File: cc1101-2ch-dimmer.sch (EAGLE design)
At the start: 24 parts, among them Q1 IRLZ44, Q2 IRLZ44, U1 ATMEGA328P-AU, U2 0ZCG0035AF2C, U3 173950378, X2 MSTBA2, X3 MSTBA2, X4 MSTBA2

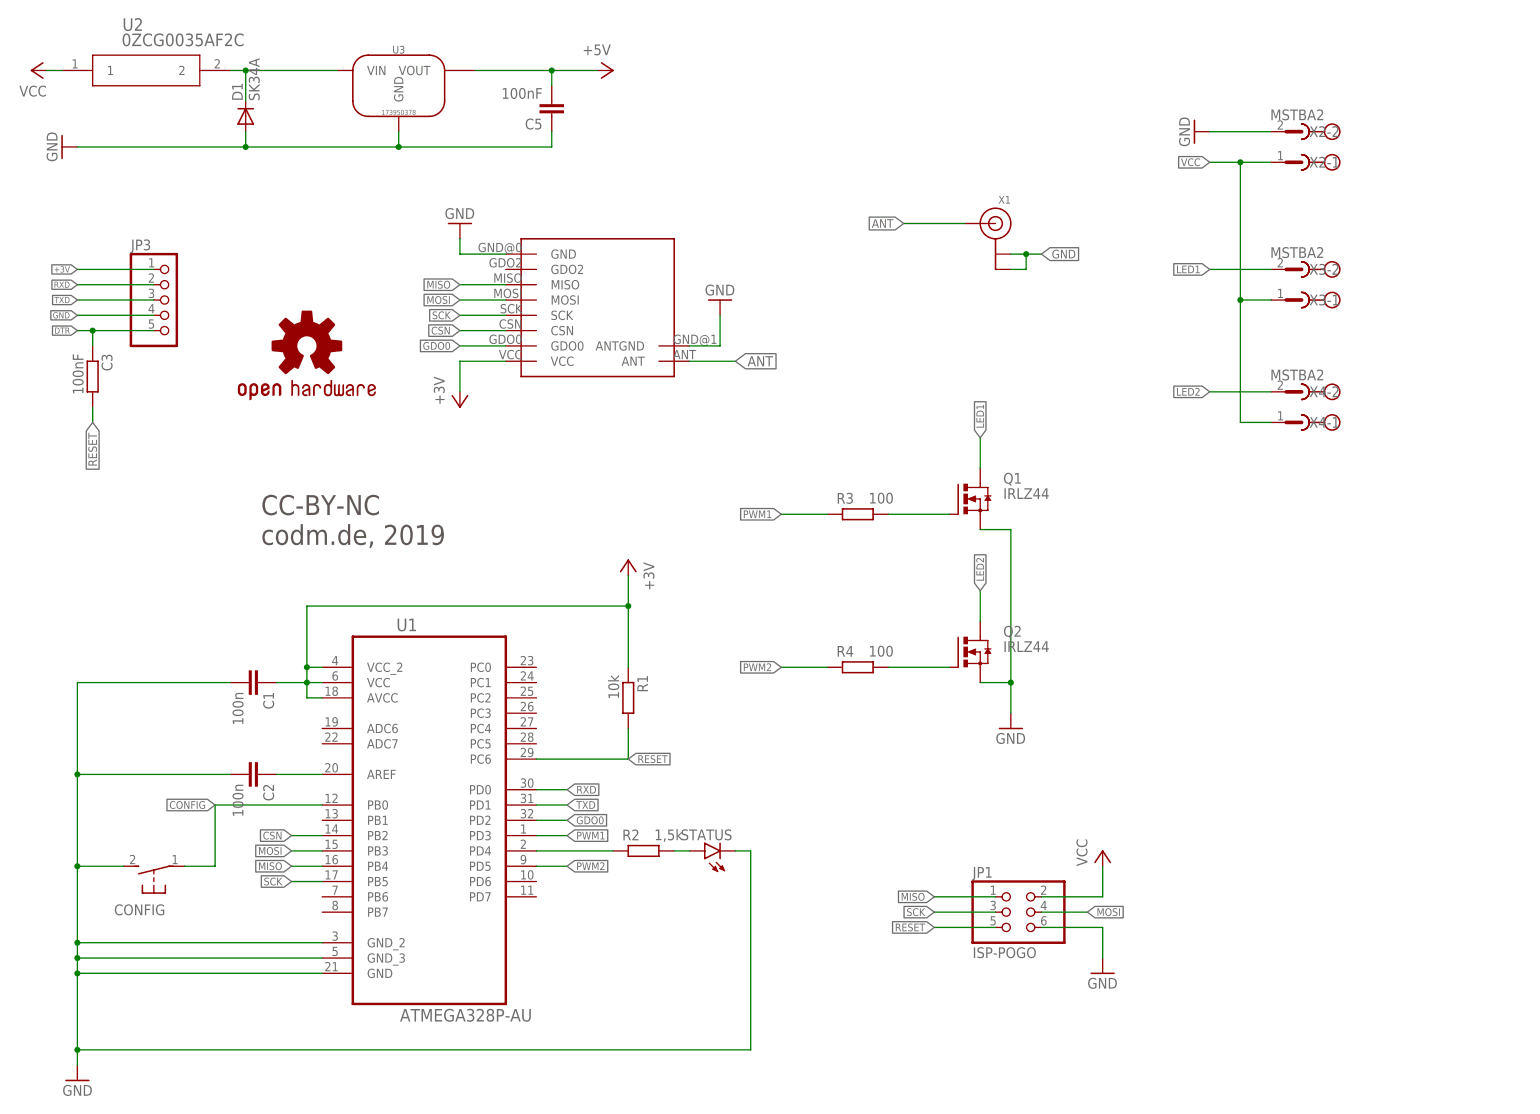
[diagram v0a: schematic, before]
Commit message: added 8mhz resonator, reworked for 0.2
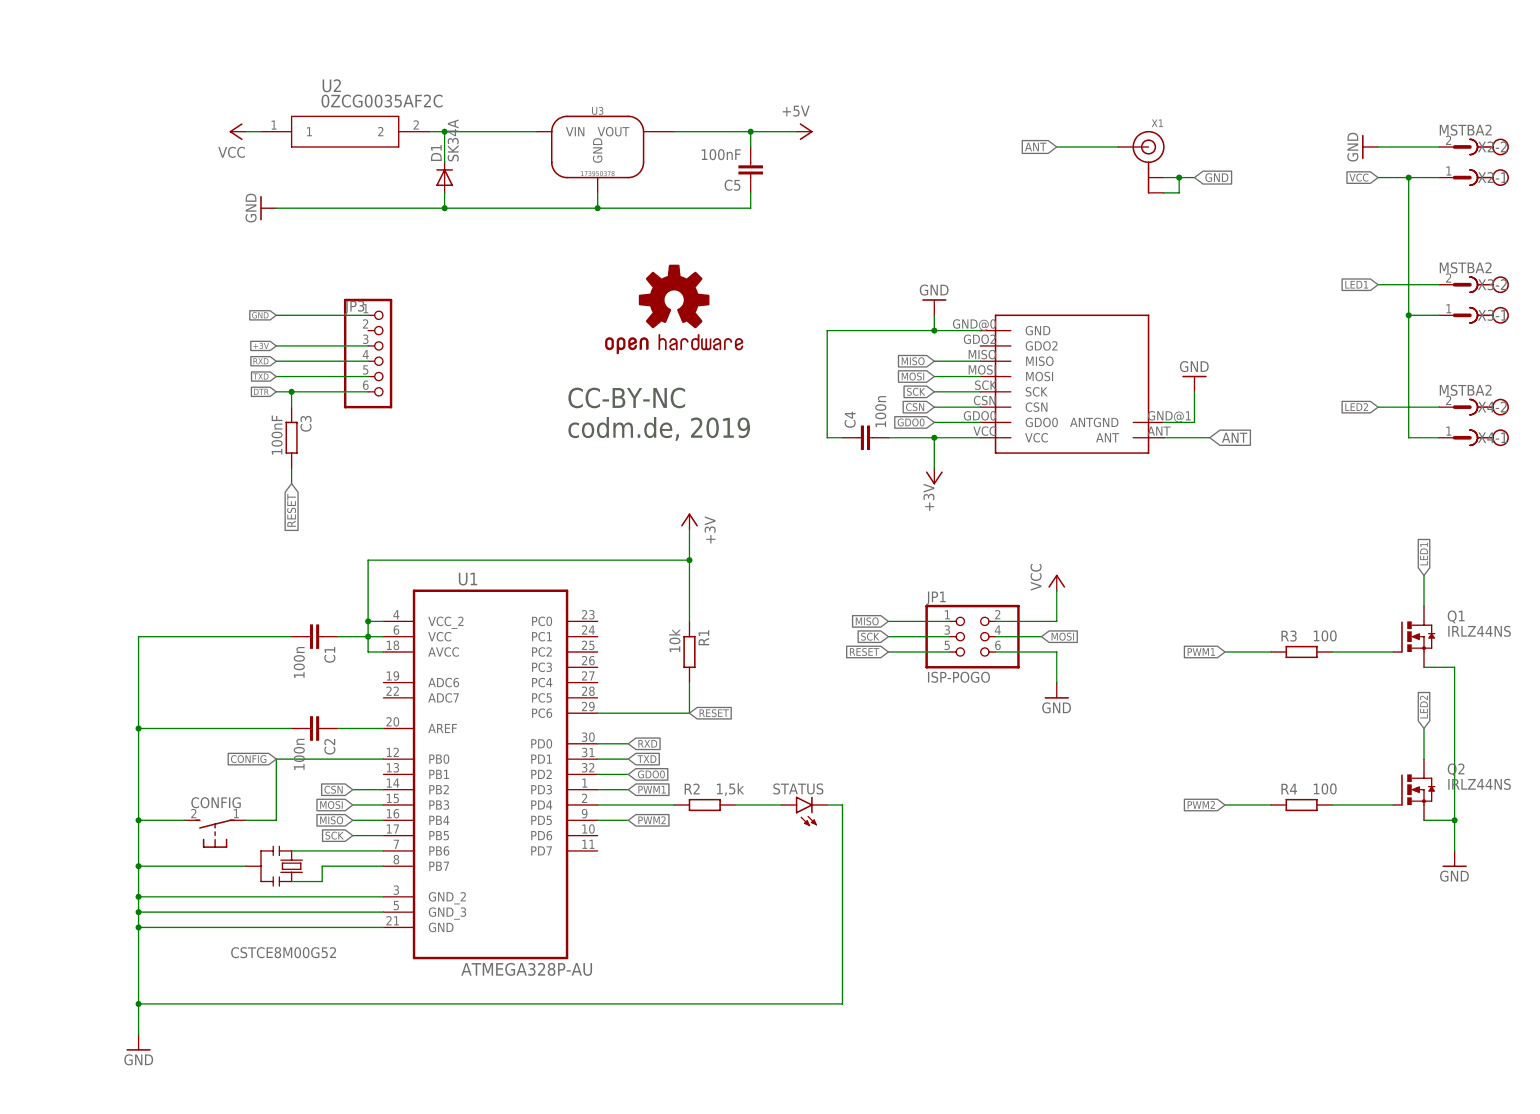
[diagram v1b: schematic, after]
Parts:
- added C4: 100n, rcl:C-EUC0805
- added Y1: CSTCE8M00G52, SmartPrj:RESONATORMU
- JP3: device pinhead:PINHD-1X5 -> pinhead:PINHD-1X6
- Q1, Q2: value IRLZ44 -> IRLZ44NS; device codm:IRFR4105ZPBF -> codm:IRLZ44NSD2PAK
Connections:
- new net N$4: U1.PB6, Y1.1
- new net N$7: U1.PB7, Y1.3
- net +3V: now also C4.2, JP3.3; no longer JP3.1
- net DTR: now also JP3.6; no longer JP3.5
- net GND: now also C4.1, JP3.1, Y1.2; no longer JP3.4
- net RXD: now also JP3.4; no longer JP3.2
- net TXD: now also JP3.5; no longer JP3.3
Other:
- moved on the sheet: C1, C2, C3, C5, CONFIG, D1, JP1, Q1, Q2, R1, R2, R3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

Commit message: reworked clearance, used newer aisler dru
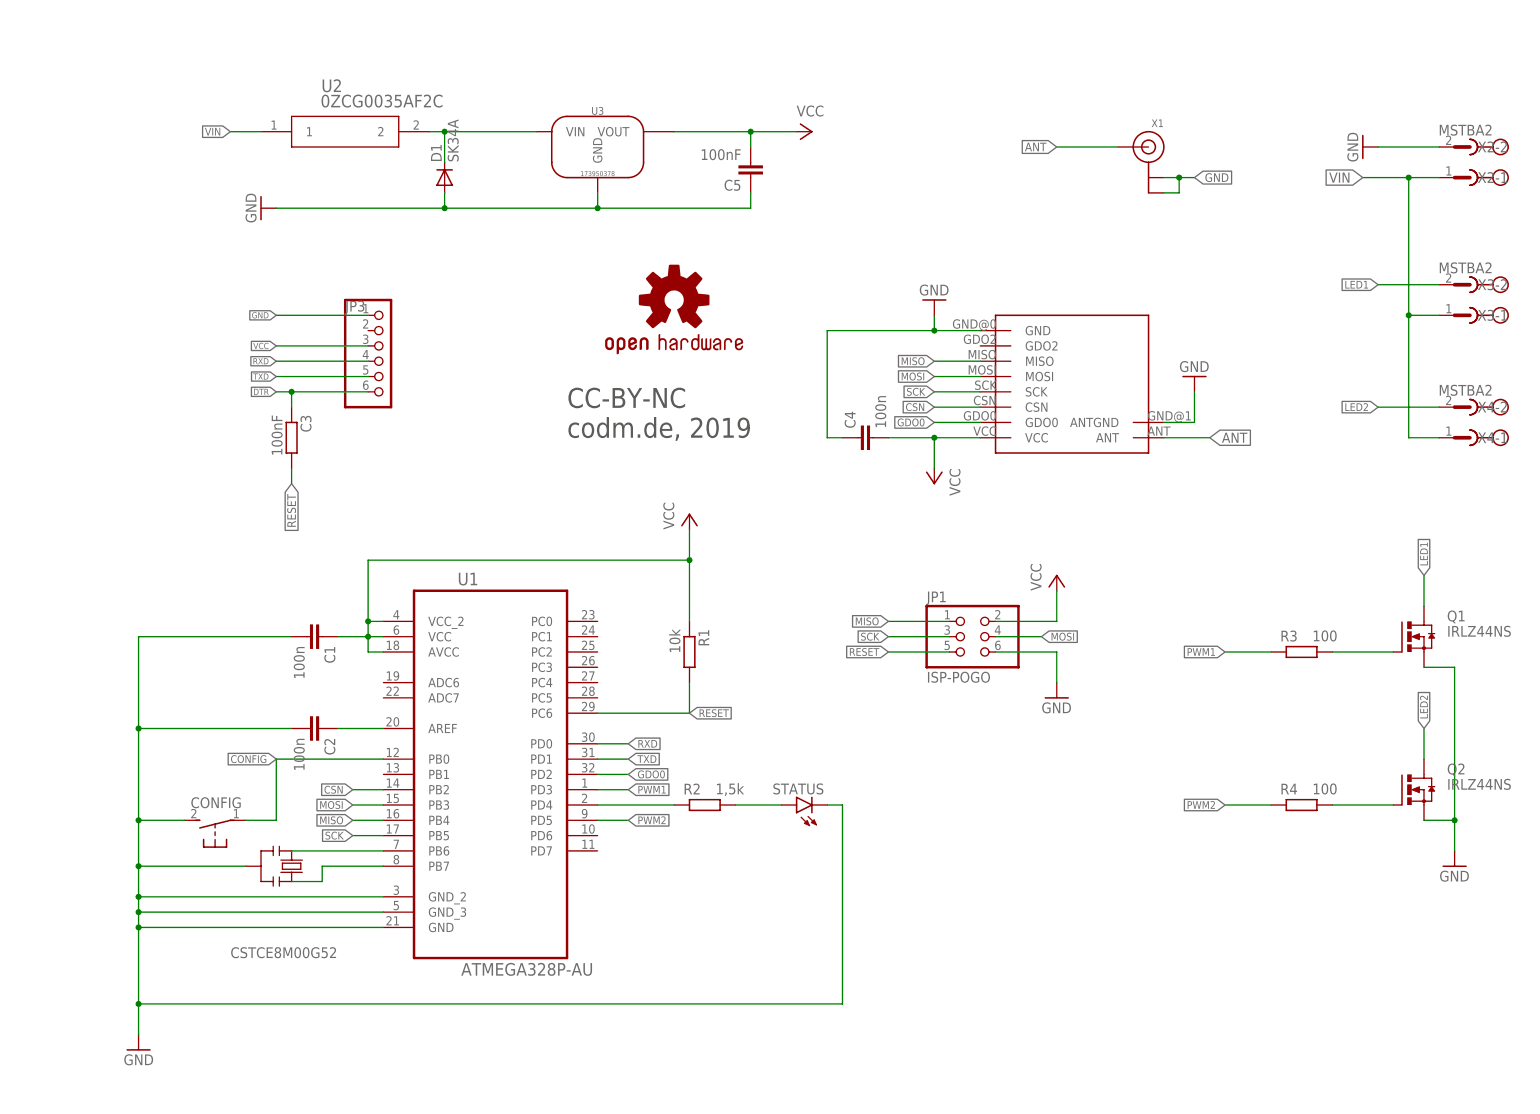
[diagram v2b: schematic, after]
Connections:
- removed net +3V: C1.1, C4.2, C5.2, JP1.2, JP3.3, R1.1, U$1.VCC, U1.AVCC, U1.VCC, U1.VCC_2, U3.VOUT
- new net VIN: U2.1, X2-1.1, X3-1.1, X4-1.1
- net VCC: now also C1.1, C4.2, C5.2, JP1.2, JP3.3, R1.1, U$1.VCC, U1.AVCC, U1.VCC, U1.VCC_2, U3.VOUT; no longer U2.1, X2-1.1, X3-1.1, X4-1.1

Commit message: added the chineses cc1101
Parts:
- added R5, R6: 0, rcl:R-EU_R0805
- added U$4: CC1101-CN-BOARD, codm:CC1101-CN-BOARD
- X1: device adafruit:ANTENNA_U.FL -> adafruit-own:ANTENNA_U.FL
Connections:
- new net ANT1: R5.1, U$1.ANT
- new net ANT2: R6.2, U$4.ANT
- net ANT: now also R5.2, R6.1; no longer U$1.ANT
- net CSN: now also U$4.CSN
- net GDO0: now also U$4.GDO0
- net GND: now also U$4.GND@1, U$4.GND@2, U$4.GND@3
- net MISO: now also U$4.MISO
- net MOSI: now also U$4.MOSI
- net SCK: now also U$4.SCLK
- net VCC: now also U$4.3V3
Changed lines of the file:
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@@
 <part name="R2" library="rcl" library_urn="urn:adsk.eagle:library:334" deviceset="R-EU_" device="R0805" package3d_urn="urn:adsk.eagle:package:23553/2" value="1,5k"/>
 <part name="STATUS" library="led" library_urn="urn:adsk.eagle:library:259" deviceset="LED" device="CHIPLED_0805" package3d_urn="urn:adsk.eagle:package:15821/2"/>
-<part name="U$1" library="codm" deviceset="CC1101-868MS10" device=""/>
+<part name="U$1" library="codm" library_urn="urn:adsk.eagle:library:11602856" deviceset="CC1101-868MS10" device="" package3d_urn="urn:adsk.eagle:package:11602923/1"/>
 <part name="GND2" library="supply1" deviceset="GND" device=""/>
 <part name="JP1" library="codm" deviceset="PINHD6-CLEAN" device="" override_package3d_urn="urn:adsk.eagle:package:11204418/2" override_package_urn="urn:adsk.eagle:footprint:11204419/1" value="ISP-POGO"/>
@@
 <part name="C1" library="rcl" library_urn="urn:adsk.eagle:library:334" deviceset="C-EU" device="C0805" package3d_urn="urn:adsk.eagle:package:23617/2" value="100n"/>
 <part name="C2" library="rcl" library_urn="urn:adsk.eagle:library:334" deviceset="C-EU" device="C0805" package3d_urn="urn:adsk.eagle:package:23617/2" value="100n"/>
-<part name="X1" library="adafruit" library_urn="urn:adsk.eagle:library:420" deviceset="ANTENNA_U.FL" device="" package3d_urn="urn:adsk.eagle:package:6240943/1" override_package3d_urn="urn:adsk.eagle:package:11204466/2" override_package_urn="urn:adsk.eagle:footprint:6240300/1"/>
+<part name="X1" library="adafruit-own" deviceset="ANTENNA_U.FL" device="" package3d_urn="urn:adsk.eagle:package:6240943/1" override_package3d_urn="urn:adsk.eagle:package:11204466/2" override_package_urn="urn:adsk.eagle:footprint:6240300/1" override_locally_modified="yes"/>
 <part name="JP3" library="pinhead" library_urn="urn:adsk.eagle:library:325" deviceset="PINHD-1X6" device="" package3d_urn="urn:adsk.eagle:package:22472/2"/>
 <part name="C3" library="rcl" library_urn="urn:adsk.eagle:library:334" deviceset="R-EU_" device="R0805" package3d_urn="urn:adsk.eagle:package:23553/2" value="100nF"/>
@@
 <part name="P+2" library="supply1" library_urn="urn:adsk.eagle:library:371" deviceset="VCC" device=""/>
 <part name="P+3" library="supply1" library_urn="urn:adsk.eagle:library:371" deviceset="VCC" device=""/>
+<part name="U$4" library="codm" library_urn="urn:adsk.eagle:library:11602856" deviceset="CC1101-CN-BOARD" device="" package3d_urn="urn:adsk.eagle:package:11602924/4"/>
+<part name="GND5" library="supply1" deviceset="GND" device=""/>
+<part name="P+4" library="supply1" library_urn="urn:adsk.eagle:library:371" deviceset="VCC" device=""/>
+<part name="R5" library="rcl" library_urn="urn:adsk.eagle:library:334" deviceset="R-EU_" device="R0805" package3d_urn="urn:adsk.eagle:package:23553/2" value="0"/>
+<part name="R6" library="rcl" library_urn="urn:adsk.eagle:library:334" deviceset="R-EU_" device="R0805" package3d_urn="urn:adsk.eagle:package:23553/2" value="0"/>
 </parts>
 <sheets>
 <sheet>
 <plain>
-<text x="86.36" y="111.76" size="3.302" layer="97">CC-BY-NC
+<text x="147.32" y="35.56" size="3.302" layer="97">CC-BY-NC
 codm.de, 2019</text>
 </plain>
@@
 <attribute name="VALUE" x="91.44" y="155.194190625" size="0.813409375" layer="96" align="bottom-center"/>
 </instance>
-<instance part="LOGO1" gate="G$1" x="104.14" y="134.62" smashed="yes"/>
+<instance part="LOGO1" gate="G$1" x="17.78" y="144.78" smashed="yes"/>
 <instance part="Y1" gate="G$1" x="40.64" y="40.64" smashed="yes">
 <attribute name="VALUE" x="30.48" y="25.4" size="1.778" layer="96"/>
@@
 <instance part="P+3" gate="VCC" x="167.64" y="88.9" smashed="yes">
 <attribute name="VALUE" x="165.1" y="86.36" size="1.778" layer="96" rot="R90"/>
+</instance>
+<instance part="U$4" gate="G$1" x="99.06" y="121.92" smashed="yes" rot="R180"/>
+<instance part="GND5" gate="1" x="116.84" y="104.14" smashed="yes" rot="MR0">
+<attribute name="VALUE" x="119.38" y="101.6" size="1.778" layer="96" rot="MR0"/>
+</instance>
+<instance part="P+4" gate="VCC" x="76.2" y="104.14" smashed="yes" rot="R180">
+<attribute name="VALUE" x="78.74" y="106.68" size="1.778" layer="96" rot="R270"/>
+</instance>
+<instance part="R5" gate="G$1" x="160.02" y="144.78" smashed="yes">
+<attribute name="NAME" x="156.464" y="146.5326" size="1.778" layer="95"/>
+<attribute name="VALUE" x="161.798" y="146.558" size="1.778" layer="96"/>
+</instance>
+<instance part="R6" gate="G$1" x="175.26" y="144.78" smashed="yes">
+<attribute name="NAME" x="171.704" y="146.5326" size="1.778" layer="95"/>
+<attribute name="VALUE" x="177.038" y="146.558" size="1.778" layer="96"/>
 </instance>
 </instances>
@@
 <pinref part="GND4" gate="1" pin="GND"/>
 </segment>
+<segment>
+<pinref part="U$4" gate="G$1" pin="GND@2"/>
+<pinref part="GND5" gate="1" pin="GND"/>
+<wire x1="111.76" y1="119.38" x2="116.84" y2="119.38" width="0.1524" layer="91"/>
+<wire x1="116.84" y1="119.38" x2="116.84" y2="109.22" width="0.1524" layer="91"/>
+<pinref part="U$4" gate="G$1" pin="GND@3"/>
+<wire x1="116.84" y1="109.22" x2="116.84" y2="106.68" width="0.1524" layer="91"/>
+<wire x1="111.76" y1="124.46" x2="116.84" y2="124.46" width="0.1524" layer="91"/>
+<wire x1="116.84" y1="124.46" x2="116.84" y2="119.38" width="0.1524" layer="91"/>
+<junction x="116.84" y="119.38"/>
+<pinref part="U$4" gate="G$1" pin="GND@1"/>
+<wire x1="78.74" y1="116.84" x2="73.66" y2="116.84" width="0.1524" layer="91"/>
+<wire x1="73.66" y1="116.84" x2="73.66" y2="109.22" width="0.1524" layer="91"/>
+<wire x1="73.66" y1="109.22" x2="116.84" y2="109.22" width="0.1524" layer="91"/>
+<junction x="116.84" y="109.22"/>
+</segment>
 </net>
 <net name="MOSI" class="0">
@@
 <wire x1="55.88" y1="50.8" x2="50.8" y2="50.8" width="0.1524" layer="91"/>
 </segment>
+<segment>
+<pinref part="U$4" gate="G$1" pin="MOSI"/>
+<wire x1="78.74" y1="119.38" x2="71.12" y2="119.38" width="0.1524" layer="91"/>
+<label x="71.12" y="119.38" size="1.27" layer="95" rot="R180" xref="yes"/>
+</segment>
 </net>
 <net name="MISO" class="0">
@@
 <wire x1="55.88" y1="48.26" x2="50.8" y2="48.26" width="0.1524" layer="91"/>
 </segment>
+<segment>
+<pinref part="U$4" gate="G$1" pin="MISO"/>
+<wire x1="78.74" y1="124.46" x2="71.12" y2="124.46" width="0.1524" layer="91"/>
+<label x="71.12" y="124.46" size="1.27" layer="95" rot="R180" xref="yes"/>
+</segment>
 </net>
 <net name="SCK" class="0">
@@
 <pinref part="JP1" gate="G$1" pin="3"/>
 <wire x1="139.7" y1="78.74" x2="149.86" y2="78.74" width="0.1524" layer="91"/>
+</segment>
+<segment>
+<pinref part="U$4" gate="G$1" pin="SCLK"/>
+<wire x1="78.74" y1="121.92" x2="71.12" y2="121.92" width="0.1524" layer="91"/>
+<label x="71.12" y="121.92" size="1.27" layer="95" rot="R180" xref="yes"/>
 </segment>
 </net>
@@
 <wire x1="91.44" y1="55.88" x2="96.52" y2="55.88" width="0.1524" layer="91"/>
 </segment>
+<segment>
+<pinref part="U$4" gate="G$1" pin="GDO0"/>
+<wire x1="78.74" y1="129.54" x2="71.12" y2="129.54" width="0.1524" layer="91"/>
+<label x="71.12" y="129.54" size="1.27" layer="95" rot="R180" xref="yes"/>
+</segment>
 </net>
 <net name="CSN" class="0">
@@
 <pinref part="U1" gate="A" pin="PB2"/>
 <wire x1="55.88" y1="53.34" x2="50.8" y2="53.34" width="0.1524" layer="91"/>
+</segment>
+<segment>
+<pinref part="U$4" gate="G$1" pin="CSN"/>
+<wire x1="78.74" y1="132.08" x2="71.12" y2="132.08" width="0.1524" layer="91"/>
+<label x="71.12" y="132.08" size="1.27" layer="95" rot="R180" xref="yes"/>
 </segment>
 </net>
@@
 <net name="ANT" class="0">
 <segment>
-<label x="167.64" y="160.02" size="1.4224" layer="95" rot="R180" xref="yes"/>
+<label x="162.56" y="160.02" size="1.4224" layer="95" rot="R180" xref="yes"/>
 <pinref part="X1" gate="G$1" pin="SIGNAL"/>
+<wire x1="162.56" y1="160.02" x2="167.64" y2="160.02" width="0.1524" layer="91"/>
+<pinref part="R5" gate="G$1" pin="2"/>
+<pinref part="R6" gate="G$1" pin="1"/>
 <wire x1="167.64" y1="160.02" x2="177.8" y2="160.02" width="0.1524" layer="91"/>
-</segment>
-<segment>
-<pinref part="U$1" gate="G$1" pin="ANT"/>
-<wire x1="185.42" y1="111.76" x2="193.04" y2="111.76" width="0.1524" layer="91"/>
-<label x="193.04" y="111.76" size="1.6764" layer="95" xref="yes"/>
+<wire x1="167.64" y1="144.78" x2="170.18" y2="144.78" width="0.1524" layer="91"/>
+<wire x1="165.1" y1="144.78" x2="167.64" y2="144.78" width="0.1524" layer="91"/>
+<wire x1="167.64" y1="144.78" x2="167.64" y2="160.02" width="0.1524" layer="91"/>
+<junction x="167.64" y="160.02"/>
 </segment>
 </net>
@@
 <pinref part="P+3" gate="VCC" pin="VCC"/>
 </segment>
+<segment>
+<pinref part="U$4" gate="G$1" pin="3V3"/>
+<pinref part="P+4" gate="VCC" pin="VCC"/>
+<wire x1="78.74" y1="114.3" x2="76.2" y2="114.3" width="0.1524" layer="91"/>
+<wire x1="76.2" y1="114.3" x2="76.2" y2="106.68" width="0.1524" layer="91"/>
+</segment>
 </net>
 <net name="N$8" class="0">
@@
 </segment>
 </net>
+<net name="ANT2" class="0">
+<segment>
+<pinref part="U$4" gate="G$1" pin="ANT"/>
+<wire x1="111.76" y1="121.92" x2="119.38" y2="121.92" width="0.1524" layer="91"/>
+<label x="119.38" y="121.92" size="1.27" layer="95" xref="yes"/>
+</segment>
+<segment>
+<pinref part="R6" gate="G$1" pin="2"/>
+<wire x1="180.34" y1="144.78" x2="185.42" y2="144.78" width="0.1524" layer="91"/>
+<label x="185.42" y="144.78" size="1.27" layer="95" xref="yes"/>
+</segment>
+</net>
+<net name="ANT1" class="0">
+<segment>
+<pinref part="U$1" gate="G$1" pin="ANT"/>
+<wire x1="185.42" y1="111.76" x2="193.04" y2="111.76" width="0.1524" layer="91"/>
+<label x="193.04" y="111.76" size="1.27" layer="95" xref="yes"/>
+</segment>
+<segment>
+<pinref part="R5" gate="G$1" pin="1"/>
+<wire x1="154.94" y1="144.78" x2="152.4" y2="144.78" width="0.1524" layer="91"/>
+<label x="152.4" y="144.78" size="1.27" layer="95" rot="R180" xref="yes"/>
+</segment>
+</net>
